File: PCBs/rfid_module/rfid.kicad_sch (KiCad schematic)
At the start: 47 parts, among them IC1701 TLV9004SIRTER, IC1702 MAX9027EBT+T, Q1701 DMN21D2UFB-7B, Q1702 DMP21D5UFB4-7B, Q1703 DMN21D2UFB-7B, Q1704 DMN21D2UFB-7B

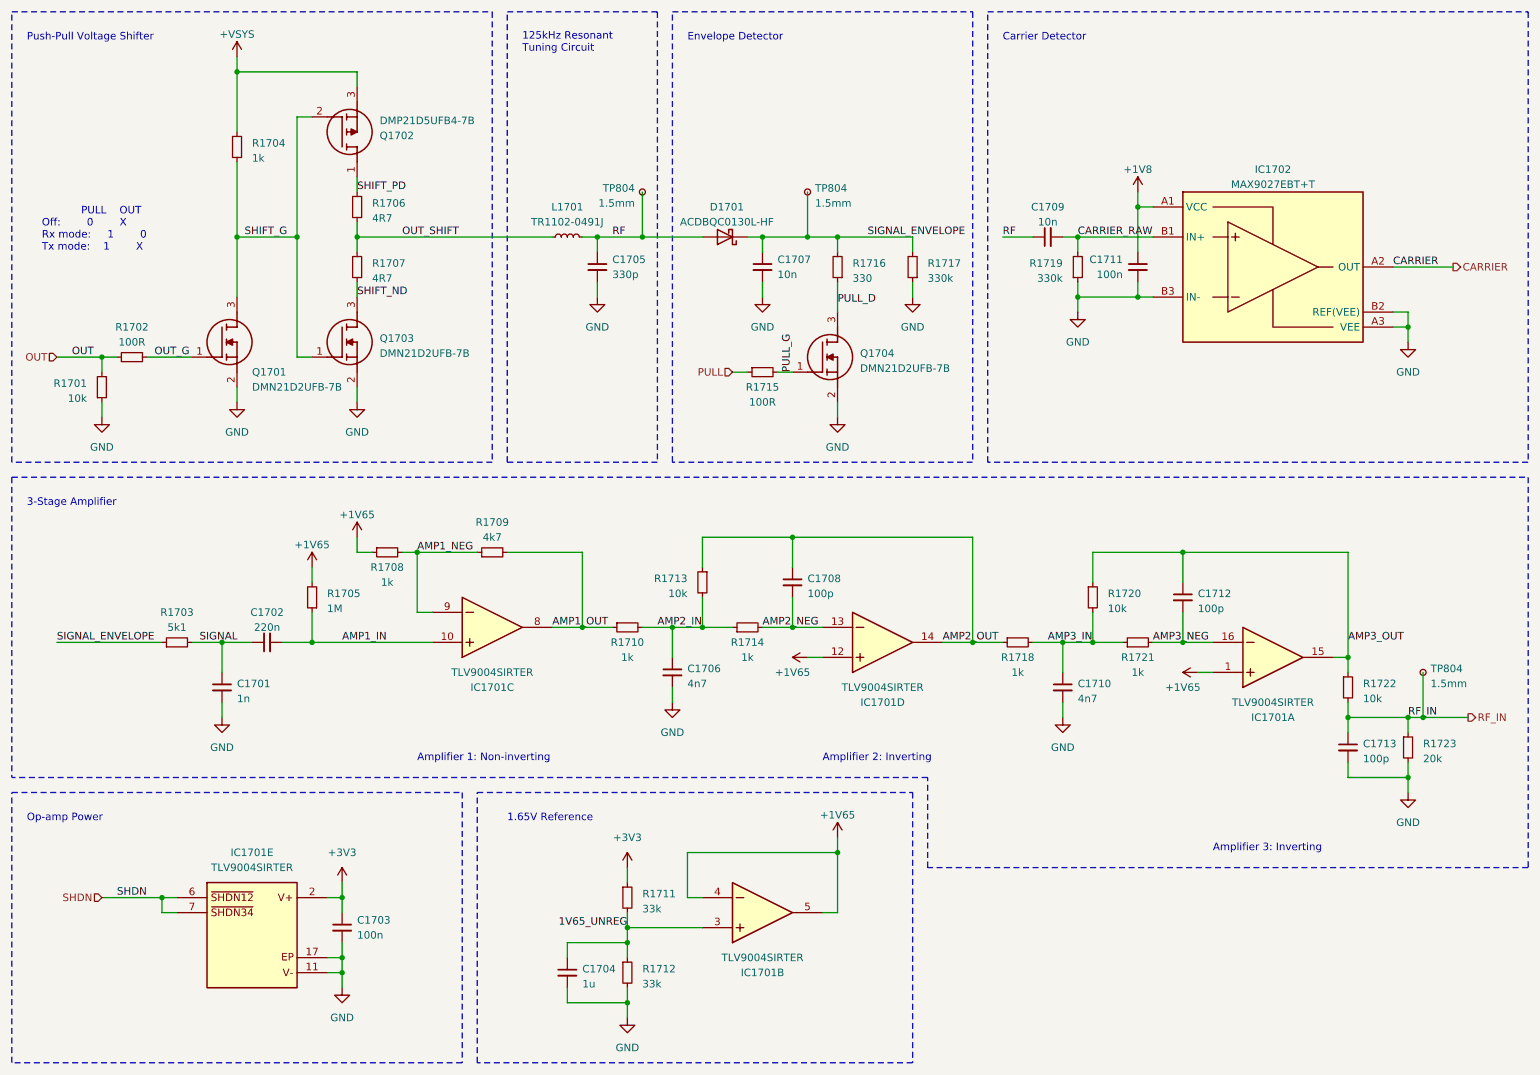
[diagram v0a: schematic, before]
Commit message: Main board and test rig complete & ordered.
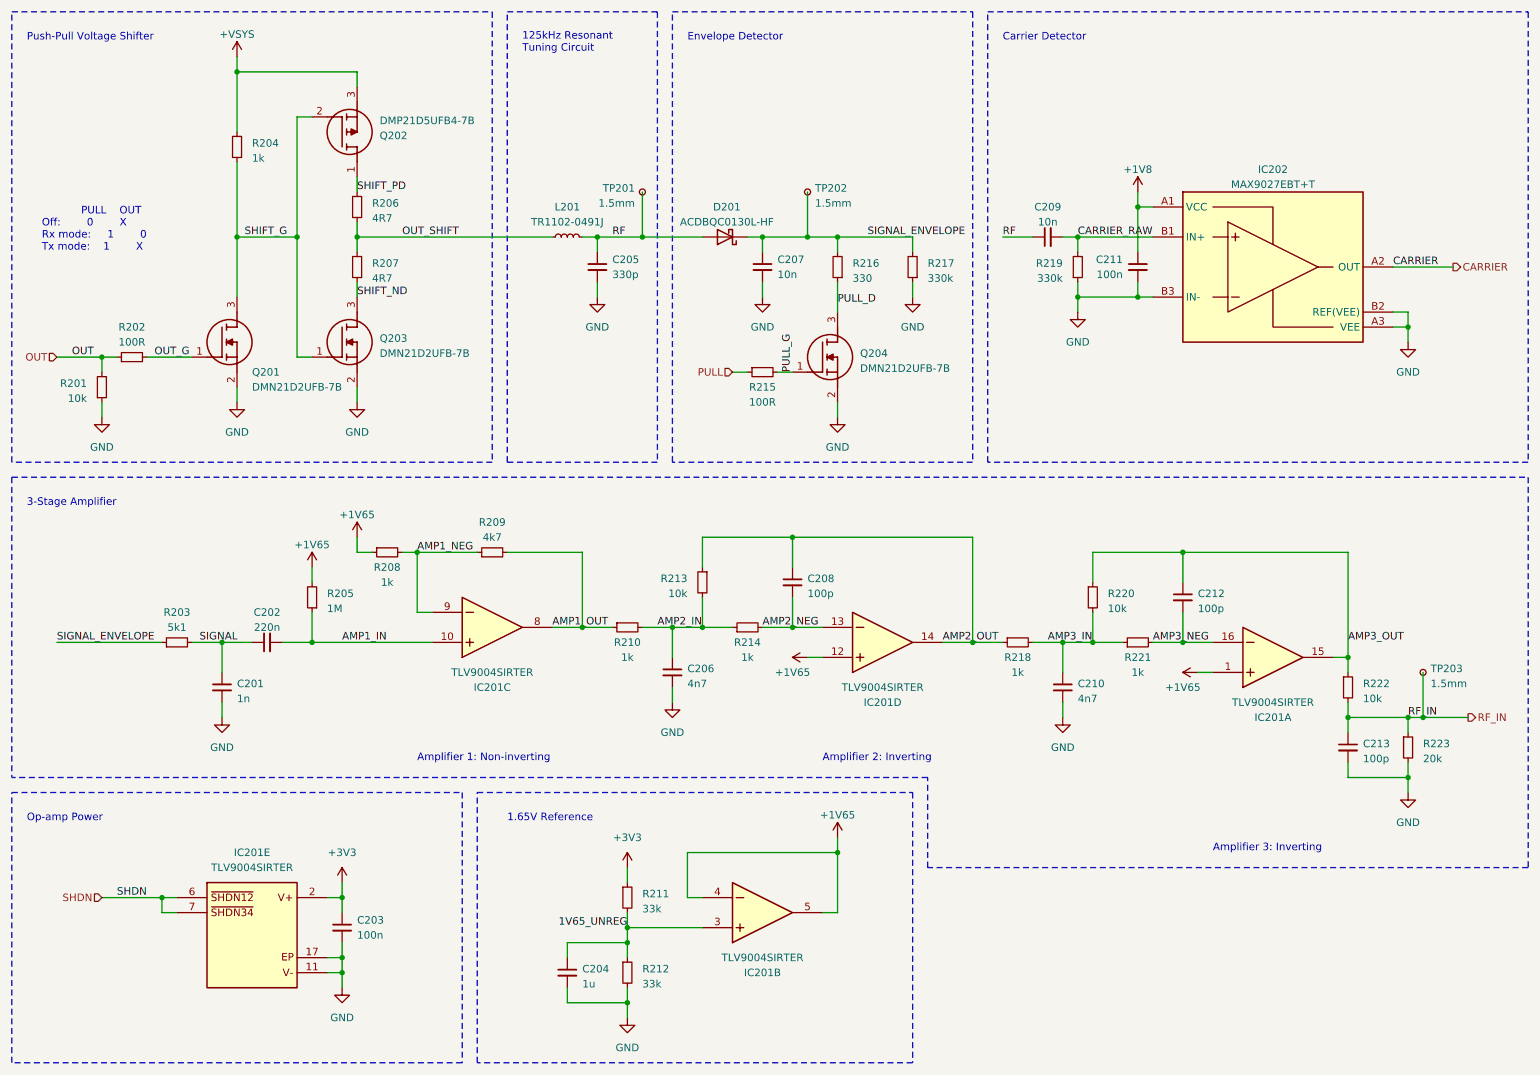
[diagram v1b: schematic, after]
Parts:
- renumbered C1701 to C201, C1702 to C202, C1703 to C203, C1704 to C204, C1705 to C205, C1706 to C206, C1707 to C207, C1708 to C208, C1709 to C209, C1710 to C210, C1711 to C211, C1712 to C212, C1713 to C213, D1701 to D201, IC1701 to IC201, IC1702 to IC202, L1701 to L201, Q1701 to Q201, Q1702 to Q202, Q1703 to Q203, Q1704 to Q204, R1701 to R201, R1702 to R202, R1703 to R203, R1704 to R204, R1705 to R205, R1706 to R206, R1707 to R207, R1708 to R208, R1709 to R209, R1710 to R210, R1711 to R211, R1712 to R212, R1713 to R213, R1714 to R214, R1715 to R215, R1716 to R216, R1717 to R217, R1718 to R218, R1719 to R219, R1720 to R220, R1721 to R221, R1722 to R222, R1723 to R223, TP804 to TP201, TP804 to TP202, TP804 to TP203

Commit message: RFID Module progress
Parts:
- R206: value 4R7 -> 100R
- R207: value 4R7 -> 10k
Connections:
- net +3V3: now also R207.2
- net OUT: now also R206.1, R207.1; no longer R201.2, R202.1
- net OUT_G: now also R206.2; no longer R202.2
- net OUT_SHIFT: now also Q202.1 (D), Q203.3 (D); no longer R206.1, R207.2
- net +VSYS renamed VRF
- net SHIFT_G renamed GATE
- net GATE: no longer Q203.1 (G)
- removed net SHIFT_ND: Q203.3 (D), R207.1
- removed net SHIFT_PD: Q202.1 (D), R206.2
- new net OUTN: R201.2, R202.1
- new net OUTN_G: Q203.1 (G), R202.2
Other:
- note added: "Dead time needs to be generated by MCU (>150ns)"
- moved on the sheet: Q201, Q202, Q203, R204

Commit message: RFID PCB Done, started lower flex PCB
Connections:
- net +1V8 is gone; now on net +3V3: C211.1, IC202.A1 (VCC)
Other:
- title: Watch RFID -> RFID Transmitter Receiver
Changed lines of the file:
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@@
   (paper "A4")
   (title_block
-    (title "Watch RFID")
-    (rev "2")
+    (title "RFID Transmitter Receiver")
+    (date "2024-01-02")
+    (rev "1")
   )
   (junction (at 246.38 134.62) (diameter 0) (color 0 0 0 0)
@@
     )
   )
+  (symbol (lib_id "power:+3V3") (at 210.82 45.72 0) (unit 1)
+    (in_bom yes) (on_board yes) (dnp no) (fields_autoplaced)
+    (property "Reference" "#PWR0204" (at 210.82 49.53 0)
+      (effects (font (size 1.27 1.27)) hide)
+    )
+    (property "Value" "+3V3" (at 210.82 41.91 0)
+      (effects (font (size 1.27 1.27)))
+    )
+    (property "Footprint" "" (at 210.82 45.72 0)
+      (effects (font (size 1.27 1.27)) hide)
+    )
+    (property "Datasheet" "" (at 210.82 45.72 0)
+      (effects (font (size 1.27 1.27)) hide)
+    )
+    (pin "1")
+    (instances
+      (project "rfid_module"
+        (path "/7f374643-2d66-4cfc-a525-255f058de0be/a9cdb386-76ee-47d2-86a0-cb7dea8af18d"
+          (reference "#PWR0204") (unit 1)
+        )
+      )
+    )
+  )
   (symbol (lib_id "Device:C_Small") (at 119.38 58.42 0) (unit 1)
     (in_bom yes) (on_board yes) (dnp no)
@@
         )
       )
-    )
-  )
-  (symbol (lib_id "power:+1V8") (at 210.82 45.72 0) (unit 1)
-    (in_bom yes) (on_board yes) (dnp no) (fields_autoplaced)
-    (property "Reference" "#PWR0221" (at 210.82 49.53 0)
-      (effects (font (size 1.27 1.27)) hide)
-    )
-    (property "Value" "+1V8" (at 210.82 41.91 0)
-      (effects (font (size 1.27 1.27)))
-    )
-    (property "Footprint" "" (at 210.82 45.72 0)
-      (effects (font (size 1.27 1.27)) hide)
-    )
-    (property "Datasheet" "" (at 210.82 45.72 0)
-      (effects (font (size 1.27 1.27)) hide)
-    )
-    (pin "1")
-    (instances
-      (project "rfid_module"
-        (path "/7f374643-2d66-4cfc-a525-255f058de0be/a9cdb386-76ee-47d2-86a0-cb7dea8af18d"
-          (reference "#PWR0221") (unit 1)
-        )
-      )
-      (project "watch_main"
-        (path "/b008648a-c7cf-4e14-8a0a-b9314d757b4a/e805c593-17ac-4f08-b6e2-d497b0af0a05"
-          (reference "#PWR01721") (unit 1)
-        )
-      )
